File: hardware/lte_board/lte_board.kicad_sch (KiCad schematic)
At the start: 105 parts, among them J1 USB-C, J2 SWD, J3 I2C_Qwiic, J4 DEBUG_UART, J5 EXPANSION, J6 LTE_ANT, J7 GNSS_ANT, J8 Nano-SIM, J9 BATTERY, Q1 MMBT3904, Q2 MMBT3904, Q3 AO3401A, Q4 AO3401A, Q5 FS8205A, SW1 RESET, SW2 BOOT0, U1 USBLC6-2SC6, U2 SY8089AAAC, U3 TPS7A0233PDBVR, U4 STM32L072CBT6, U5 TXS0108EPWR, U6 SIM7080G, U7 ESDA6V1W5, U8 MAX17048G+T10, U9 DW01A

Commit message: Pre-fab audit fixes (rev 0.4) and antenna rework (rev 0.5)
Rev 0.4, from the independent design audit:
- No vias in SMD pads: stitch.py, final_fixes.py and maze_route.py keep vias
  0.1 mm clear of every SMD pad, the DSN sets via_at_smd off, and the new
  check_via_in_pad.py runs at the end of pipeline.sh (0 found).
- JLC rotations: make_jlc.py applies a per-LCSC-number JLC_CORR table
  (rotation + origin offset fitted against each part's EasyEDA footprint),
  and fails on a non-passive part without an entry. Fixes J9 polarity.
- 32.768 kHz LSE crystal Y1 (Seiko SC-32S, 7 pF, C97604) with 10 pF C54/C55
  on PC14/PC15.
- L1 on Sunlord's recommended SWPA4030S land (new footprint).
- AN2606 checked: the L072 ROM bootloader needs no extra pull-ups.

Rev 0.5, antennas (SIM7080G Hardware Design V1.05 section 4):
- LTE: C61 100 pF series + D6 ESD103-B1-02EL after the R19/C40/C41 match;
  U.FL J6 fitted, optional Amphenol 132322 edge SMA J10 via DNP R40 0R.
- GNSS: SMA J7 (Amphenol 132322, hand-soldered) with an active-antenna bias
  tee: C56 100 pF DC block, L2 47 nH (LQW15AN, SRF >= 2.9 GHz) + R38 10R,
  D5 WE05DGCF-B, C58/C59 DNP match shunts.
- Antenna supply: U10 TPS22945 (100-200 mA limit) from +3V3, ON = PA15
  (R39 pull-down), OC flag -> PB3.
- No In1/In2 copper under the SMA centre pads; modem USB vias moved to free
  a lane for the SMA-option trace; SW1, TP3, JP1 moved.
- sch_rev04.py / sch_rev05.py hold the schematic edits; DESIGN.md,
  README.md and DATASHEETS.md updated.

Verified: ERC 0; DRC 0 violations / 0 unconnected / 0 parity; vias in SMD
pads 0; BOM 50 lines / 104 parts, CPL 104, no mismatches.

Co-Authored-By: Claude Opus 5.5 <noreply@anthropic.com>
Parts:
- added C54, C55: 10pF, Capacitor_SMD:C_0402_1005Metric, symbol lte_board:C
- added C56, C61: 100pF, Capacitor_SMD:C_0402_1005Metric, symbol lte_board:C
- added C57, C60: 100nF, Capacitor_SMD:C_0402_1005Metric, symbol lte_board:C
- added C58, C59: DNP, Capacitor_SMD:C_0402_1005Metric, symbol lte_board:C
- added D5: WE05DGCF-B, lte_board_lcsc:DFN1006-2L-BI, symbol lte_board:D_TVS
- added D6: ESD103-B1-02EL, lte_board_lcsc:TSLP-2-20_L1.0-W0.6-P0.65-BI, symbol lte_board:D_TVS
- added J10: LTE_ANT (SMA), lte_board_lcsc:SMA_Amphenol_132322_EdgeMount, symbol lte_board:U.FL
- added L2: 47nH, Inductor_SMD:L_0402_1005Metric, symbol lte_board:L
- added R38: 10R, Resistor_SMD:R_0402_1005Metric, symbol lte_board:R
- added R39: 100k, Resistor_SMD:R_0402_1005Metric, symbol lte_board:R
- added R40: 0R, Resistor_SMD:R_0402_1005Metric, symbol lte_board:R
- added U10: TPS22945, lte_board_lcsc:SC-70-5_L2.1-W1.3-P0.65-LS2.1-BL, symbol lte_board:TPS22945
- added Y1: 32.768kHz, Crystal:Crystal_SMD_3215-2Pin_3.2x1.5mm, symbol lte_board:Crystal
- J7: value GNSS_ANT -> GNSS_ANT (SMA); footprint Connector_Coaxial:U.FL_Hirose_U.FL-R-SMT-1_Vertical -> lte_board_lcsc:SMA_Amphenol_132322_EdgeMount; LCSC C88374 -> C42394535; MPN U.FL-R-SMT-1(80) -> Amphenol 132322; now left out of the parts list
- L1: footprint Inductor_SMD:L_Wuerth_MAPI-4030 -> lte_board_lcsc:L_Sunlord_SWPA4030S
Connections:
- net +3V3: now also C60.1, U10.5 (VIN)
- net GND: now also C54.2, C55.2, C57.2, C58.2, C59.2, C60.2, D5.2 (A2), D6.2 (A2), J10.2 (GND), R39.2, U10.2 (GND)
- net GNSS_ANT: now also C56.2, D5.1 (A1), L2.1; no longer R20.2
- net LTE_ANT: now also C61.2, D6.1 (A1), R40.1; no longer C41.1, R19.2
- net MDM_GNSS: now also C59.1
- net OSC32_IN: now reaches U4.3 (PC14-OSC32_IN)
- net OSC32_IN: now also C54.1, Y1.1
- net GNSS_ANT_EN: now reaches U4.38 (PA15)
- net GNSS_ANT_EN: now also R39.1, U10.4 (ON)
- net GNSS_ANT_FLT: now reaches U4.39 (PB3)
- net GNSS_ANT_FLT: now also U10.3 (OC)
- net OSC32_OUT: now reaches U4.4 (PC15-OSC32_OUT)
- net OSC32_OUT: now also C55.1, Y1.2
- new net GNSS_BIAS: L2.2, R38.1
- new net GNSS_MATCH: C56.1, C58.1, R20.2
- new net GNSS_VANT: C57.1, R38.2, U10.1 (VOUT)
- new net LTE_MATCH: C41.1, C61.1, R19.2
- new net LTE_SMA: J10.1 (SIG), R40.2
- no-connect marks 47 -> 43

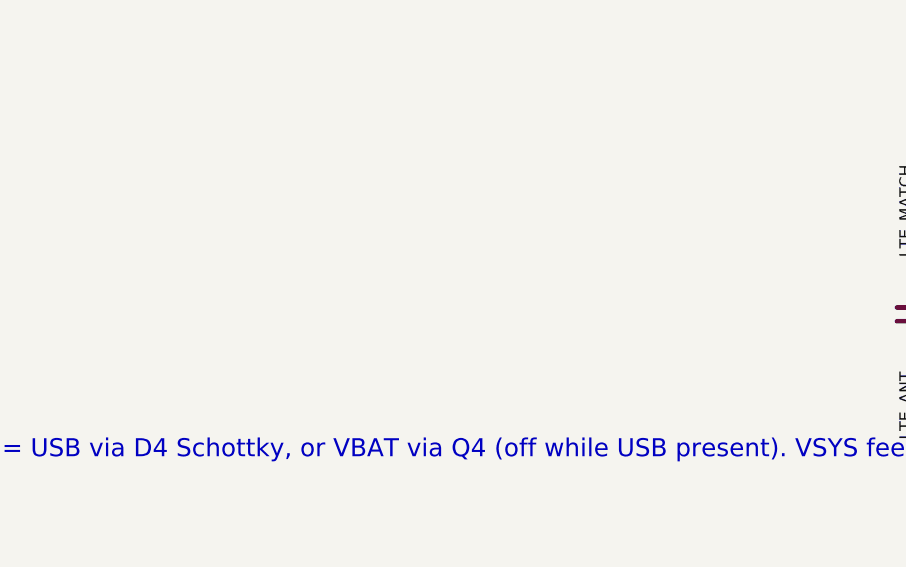
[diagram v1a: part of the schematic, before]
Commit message: lte_board rev 0.6: impedance widths for JLC default stackup, audit H10 fixes
- RF traces 0.30 mm (~49 ohm), modem USB pair 0.25/0.20 mm (~92 ohm diff)
  on JLC04161H-7628 (no impedance control ordered)
- H10a: C62 100 nF at U5 VCCA
- H10d: SIM caps C50-C53 and ESD array U7 moved next to the holder
- H10e: keep-out over the SIM7080G forbidden area (HD V1.05 Fig. 4)
- H10g: D7 ESD5651N-2/TR VBAT TVS, D8 WE05DGCF-B on PWRKEY
- H10h: C1 10 uF 25 V 0805 (C15850)
- crystal Y1 copper keep-out; MAX17048 land per Maxim 90-0065
- RESET/BOOT0 silkscreen labels on SW1/SW2
- docs: stackup/impedance, LSE drive must be medium-high or high

ERC 0; DRC 0/0/0 with schematic parity; BOM/CPL 107/107.

Co-Authored-By: Claude Opus 5.5 <noreply@anthropic.com>
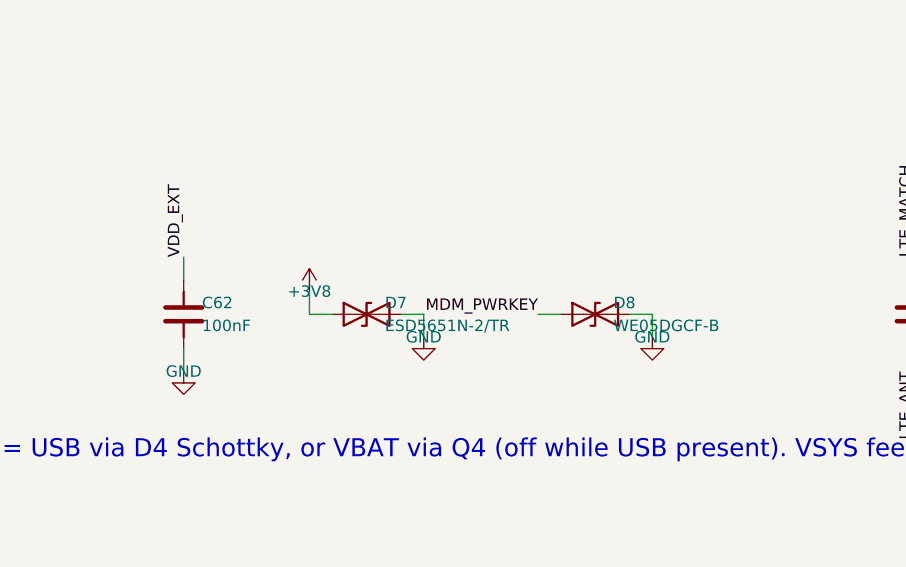
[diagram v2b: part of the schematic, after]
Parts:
- added C62: 100nF, Capacitor_SMD:C_0402_1005Metric, symbol lte_board:C
- added D7: ESD5651N-2/TR, lte_board_lcsc:DFN1006-2L-BI-1, symbol lte_board:D_TVS
- added D8: WE05DGCF-B, lte_board_lcsc:DFN1006-2L-BI, symbol lte_board:D_TVS
- C1: footprint Capacitor_SMD:C_0603_1608Metric -> Capacitor_SMD:C_0805_2012Metric; LCSC C19702 -> C15850; MPN CL10A106KP8NNNC -> CL21A106KAYNNNE
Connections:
- net +3V8: now also D7.1 (A1)
- net GND: now also C62.2, D7.2 (A2), D8.2 (A2)
- net MDM_PWRKEY: now also D8.1 (A1)
- net VDD_EXT: now also C62.1
